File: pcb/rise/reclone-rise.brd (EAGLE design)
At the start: 85 x 56 mm, 13 parts, among them J1 MAGJACK, U1 6SLX16FTG256

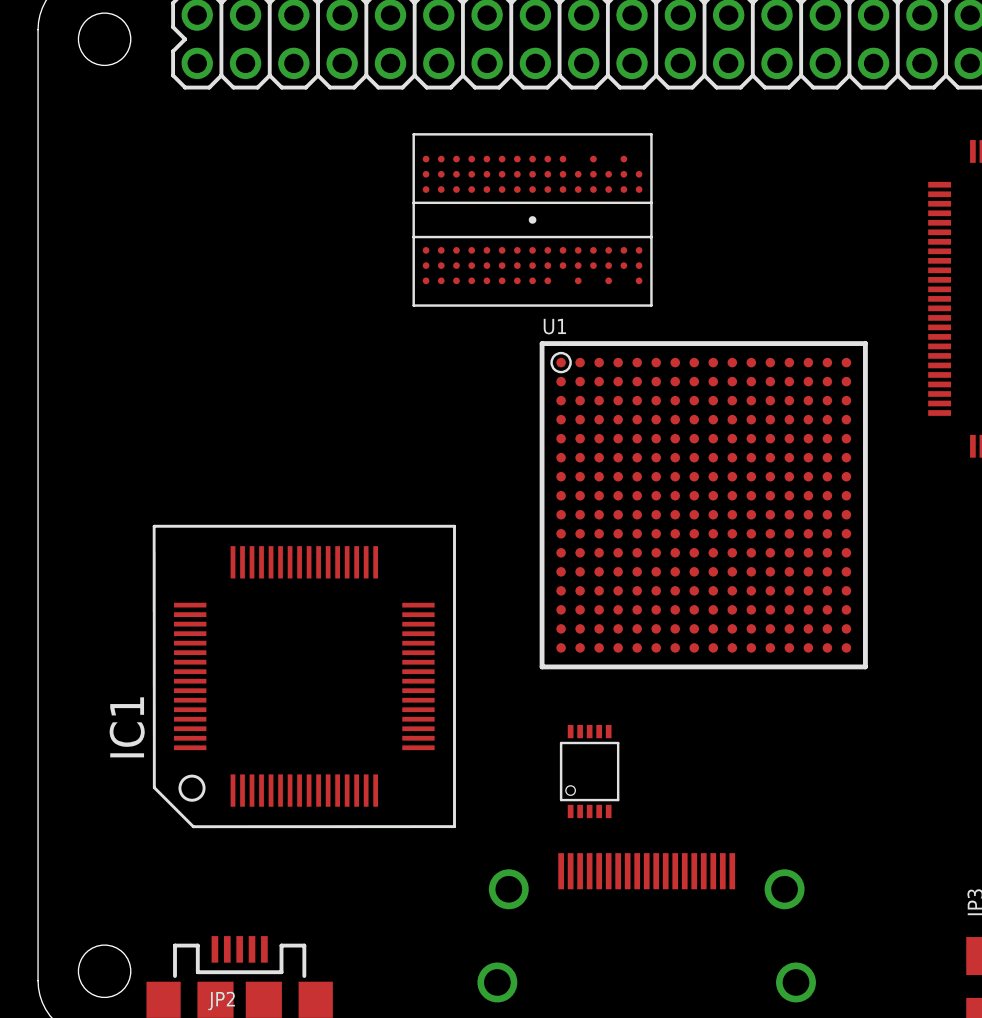
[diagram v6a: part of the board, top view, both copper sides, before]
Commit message: Added microSD socket as a placeholder
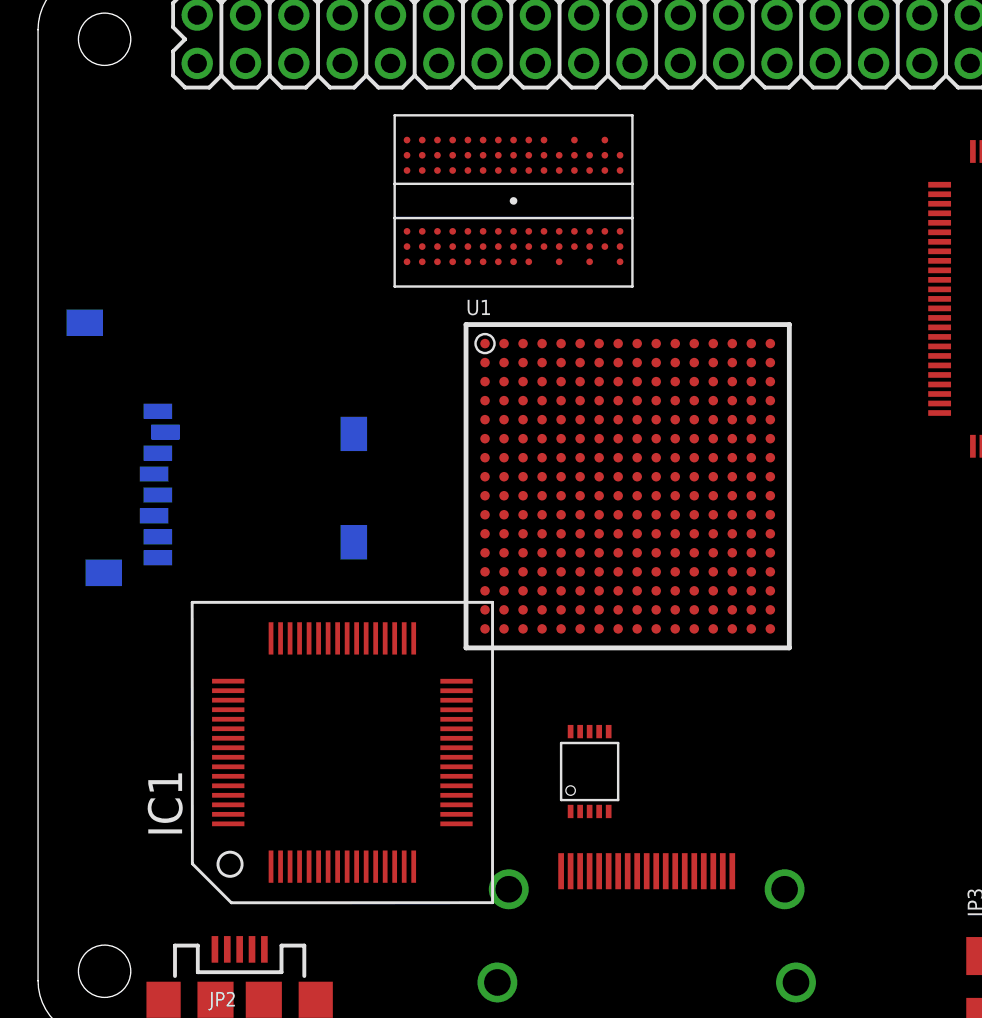
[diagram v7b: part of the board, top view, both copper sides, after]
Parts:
- added U2: USD-SOCKETNEW, SparkFun-Connectors:MICRO-SD-SOCKET-PP
- moved IC1 4.47 mm to (16.0, 15.0)
- moved U1 4.12 mm to (31.0, 29.0)
- moved U$5 1.41 mm to (25.0, 44.0)
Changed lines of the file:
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@@
 <element name="JP1" library="SparkFun-Connectors" package="2X20" value="M20X2" x="32.5" y="52.5" locked="yes"/>
 <element name="J1" library="SparkFun-Connectors" package="MAGJACK" value="MAGJACK" x="86" y="2.25" locked="yes" rot="R90"/>
-<element name="IC1" library="ftdichip-3" package="TQFP64-12X12" value="" x="14" y="19"/>
+<element name="IC1" library="ftdichip-3" package="TQFP64-12X12" value="" x="16" y="15"/>
 <element name="JP2" library="SparkFun-Connectors" package="USB-MICROB" value="USB-MICROB" x="10.6" y="2" locked="yes">
 <attribute name="PROD_ID" value="CONN-09505" x="10.6" y="2" size="1.778" layer="27" display="off"/>
@@
 <element name="U$2" library="reclone-rise" package="LQFP-48" value="DP83848C" x="57" y="23"/>
 <element name="U$3" library="reclone-rise" package="HDMI_A_SMT" value="HDMI_A" x="32" y="4" locked="yes" rot="R270"/>
-<element name="U1" library="xilinx_devices_V6" package="FT256" value="6SLX16FTG256" x="35" y="28"/>
+<element name="U1" library="xilinx_devices_V6" package="FT256" value="6SLX16FTG256" x="31" y="29"/>
 <element name="U$4" library="Gadgeteer" package="SHF105DSM_1" value="SHF105" x="76" y="46"/>
-<element name="U$5" library="reclone-rise" package="84-FBGA-9X12.5" value="MT47H128M16" x="26" y="43" rot="R90"/>
+<element name="U$5" library="reclone-rise" package="84-FBGA-9X12.5" value="MT47H128M16" x="25" y="44" rot="R90"/>
+<element name="U2" library="SparkFun-Connectors" package="MICRO-SD-SOCKET-PP" value="USD-SOCKETNEW" x="17" y="24" rot="MR270">
+<attribute name="PROD_ID" value="CONN-07820" x="17" y="24" size="1.778" layer="28" rot="MR270" display="off"/>
+</element>
 </elements>
 <signals>
@@
 <contactref element="U1" pad="T1"/>
 <contactref element="U1" pad="T16"/>
-<wire x1="16.7501" y1="25.0001" x2="20.0001" y2="19.25" width="0" layer="19" extent="1-1"/>
-<wire x1="10.7499" y1="25.0001" x2="16.7501" y2="25.0001" width="0" layer="19" extent="1-1"/>
-<wire x1="7.9999" y1="21.75" x2="10.7499" y2="25.0001" width="0" layer="19" extent="1-1"/>
-<wire x1="17.25" y1="12.9999" x2="20.0001" y2="19.25" width="0" layer="19" extent="1-1"/>
-<wire x1="15.25" y1="12.9999" x2="17.25" y2="12.9999" width="0" layer="19" extent="1-1"/>
-<wire x1="12.25" y1="12.9999" x2="15.25" y2="12.9999" width="0" layer="19" extent="1-1"/>
-<wire x1="10.25" y1="12.9999" x2="12.25" y2="12.9999" width="0" layer="19" extent="1-1"/>
-<wire x1="42.5" y1="35.5" x2="7.9999" y2="21.75" width="0" layer="19" extent="1-1"/>
-<wire x1="39.5" y1="32.5" x2="42.5" y2="35.5" width="0" layer="19" extent="1-1"/>
-<wire x1="37.5" y1="34.5" x2="39.5" y2="32.5" width="0" layer="19" extent="1-1"/>
-<wire x1="41.5" y1="29.5" x2="39.5" y2="32.5" width="0" layer="19" extent="1-1"/>
-<wire x1="38.5" y1="28.5" x2="41.5" y2="29.5" width="0" layer="19" extent="1-1"/>
-<wire x1="35.5" y1="28.5" x2="38.5" y2="28.5" width="0" layer="19" extent="1-1"/>
-<wire x1="34.5" y1="27.5" x2="35.5" y2="28.5" width="0" layer="19" extent="1-1"/>
-<wire x1="33.5" y1="28.5" x2="34.5" y2="27.5" width="0" layer="19" extent="1-1"/>
-<wire x1="33.5" y1="26.5" x2="34.5" y2="27.5" width="0" layer="19" extent="1-1"/>
-<wire x1="35.5" y1="26.5" x2="34.5" y2="27.5" width="0" layer="19" extent="1-1"/>
-<wire x1="34.5" y1="29.5" x2="35.5" y2="28.5" width="0" layer="19" extent="1-1"/>
-<wire x1="31.5" y1="27.5" x2="33.5" y2="28.5" width="0" layer="19" extent="1-1"/>
-<wire x1="34.5" y1="24.5" x2="33.5" y2="26.5" width="0" layer="19" extent="1-1"/>
-<wire x1="35.5" y1="31.5" x2="34.5" y2="29.5" width="0" layer="19" extent="1-1"/>
-<wire x1="28.5" y1="25.5" x2="31.5" y2="27.5" width="0" layer="19" extent="1-1"/>
-<wire x1="29.5" y1="22.5" x2="28.5" y2="25.5" width="0" layer="19" extent="1-1"/>
-<wire x1="27.5" y1="20.5" x2="29.5" y2="22.5" width="0" layer="19" extent="1-1"/>
-<wire x1="32.5" y1="21.5" x2="29.5" y2="22.5" width="0" layer="19" extent="1-1"/>
-<wire x1="28.5" y1="29.5" x2="31.5" y2="27.5" width="0" layer="19" extent="1-1"/>
-<wire x1="36.5" y1="21.5" x2="34.5" y2="24.5" width="0" layer="19" extent="1-1"/>
-<wire x1="33.5" y1="34.5" x2="35.5" y2="31.5" width="0" layer="19" extent="1-1"/>
-<wire x1="30.5" y1="32.5" x2="28.5" y2="29.5" width="0" layer="19" extent="1-1"/>
-<wire x1="39.5" y1="23.5" x2="36.5" y2="21.5" width="0" layer="19" extent="1-1"/>
-<wire x1="41.5" y1="25.5" x2="39.5" y2="23.5" width="0" layer="19" extent="1-1"/>
-<wire x1="27.5" y1="35.5" x2="30.5" y2="32.5" width="0" layer="19" extent="1-1"/>
-<wire x1="42.5" y1="20.5" x2="39.5" y2="23.5" width="0" layer="19" extent="1-1"/>
+<wire x1="18.7501" y1="21.0001" x2="22.0001" y2="15.25" width="0" layer="19" extent="1-1"/>
+<wire x1="12.7499" y1="21.0001" x2="18.7501" y2="21.0001" width="0" layer="19" extent="1-1"/>
+<wire x1="9.9999" y1="17.75" x2="12.7499" y2="21.0001" width="0" layer="19" extent="1-1"/>
+<wire x1="19.25" y1="8.9999" x2="22.0001" y2="15.25" width="0" layer="19" extent="1-1"/>
+<wire x1="17.25" y1="8.9999" x2="19.25" y2="8.9999" width="0" layer="19" extent="1-1"/>
+<wire x1="14.25" y1="8.9999" x2="17.25" y2="8.9999" width="0" layer="19" extent="1-1"/>
+<wire x1="12.25" y1="8.9999" x2="14.25" y2="8.9999" width="0" layer="19" extent="1-1"/>
+<wire x1="38.5" y1="36.5" x2="9.9999" y2="17.75" width="0" layer="19" extent="1-1"/>
+<wire x1="35.5" y1="33.5" x2="38.5" y2="36.5" width="0" layer="19" extent="1-1"/>
+<wire x1="33.5" y1="35.5" x2="35.5" y2="33.5" width="0" layer="19" extent="1-1"/>
+<wire x1="37.5" y1="30.5" x2="35.5" y2="33.5" width="0" layer="19" extent="1-1"/>
+<wire x1="34.5" y1="29.5" x2="37.5" y2="30.5" width="0" layer="19" extent="1-1"/>
+<wire x1="31.5" y1="29.5" x2="34.5" y2="29.5" width="0" layer="19" extent="1-1"/>
+<wire x1="30.5" y1="28.5" x2="31.5" y2="29.5" width="0" layer="19" extent="1-1"/>
+<wire x1="29.5" y1="29.5" x2="30.5" y2="28.5" width="0" layer="19" extent="1-1"/>
+<wire x1="29.5" y1="27.5" x2="30.5" y2="28.5" width="0" layer="19" extent="1-1"/>
+<wire x1="31.5" y1="27.5" x2="30.5" y2="28.5" width="0" layer="19" extent="1-1"/>
+<wire x1="30.5" y1="30.5" x2="31.5" y2="29.5" width="0" layer="19" extent="1-1"/>
+<wire x1="27.5" y1="28.5" x2="29.5" y2="29.5" width="0" layer="19" extent="1-1"/>
+<wire x1="30.5" y1="25.5" x2="29.5" y2="27.5" width="0" layer="19" extent="1-1"/>
+<wire x1="31.5" y1="32.5" x2="30.5" y2="30.5" width="0" layer="19" extent="1-1"/>
+<wire x1="24.5" y1="26.5" x2="27.5" y2="28.5" width="0" layer="19" extent="1-1"/>
+<wire x1="25.5" y1="23.5" x2="24.5" y2="26.5" width="0" layer="19" extent="1-1"/>
+<wire x1="23.5" y1="21.5" x2="25.5" y2="23.5" width="0" layer="19" extent="1-1"/>
+<wire x1="28.5" y1="22.5" x2="25.5" y2="23.5" width="0" layer="19" extent="1-1"/>
+<wire x1="24.5" y1="30.5" x2="27.5" y2="28.5" width="0" layer="19" extent="1-1"/>
+<wire x1="32.5" y1="22.5" x2="30.5" y2="25.5" width="0" layer="19" extent="1-1"/>
+<wire x1="29.5" y1="35.5" x2="31.5" y2="32.5" width="0" layer="19" extent="1-1"/>
+<wire x1="26.5" y1="33.5" x2="24.5" y2="30.5" width="0" layer="19" extent="1-1"/>
+<wire x1="35.5" y1="24.5" x2="32.5" y2="22.5" width="0" layer="19" extent="1-1"/>
+<wire x1="37.5" y1="26.5" x2="35.5" y2="24.5" width="0" layer="19" extent="1-1"/>
+<wire x1="23.5" y1="36.5" x2="26.5" y2="33.5" width="0" layer="19" extent="1-1"/>
+<wire x1="38.5" y1="21.5" x2="35.5" y2="24.5" width="0" layer="19" extent="1-1"/>
 </signal>
 <signal name="AGND">
@@
 <contactref element="IC1" pad="37"/>
 <contactref element="IC1" pad="64"/>
-<wire x1="15.7499" y1="12.9999" x2="15.7501" y2="25.0001" width="0" layer="19" extent="1-1"/>
-<wire x1="7.9999" y1="15.2499" x2="15.7499" y2="12.9999" width="0" layer="19" extent="1-1"/>
+<wire x1="17.7499" y1="8.9999" x2="17.7501" y2="21.0001" width="0" layer="19" extent="1-1"/>
+<wire x1="9.9999" y1="11.2499" x2="17.7499" y2="8.9999" width="0" layer="19" extent="1-1"/>
 </signal>
 <signal name="VCCIO">
@@
 <contactref element="IC1" pad="42"/>
 <contactref element="IC1" pad="56"/>
-<wire x1="20.0001" y1="16.7501" x2="20.0001" y2="22.2469" width="0" layer="19" extent="1-1"/>
-<wire x1="13.25" y1="25.0001" x2="20.0001" y2="22.2469" width="0" layer="19" extent="1-1"/>
-<wire x1="7.9999" y1="19.2501" x2="13.25" y2="25.0001" width="0" layer="19" extent="1-1"/>
+<wire x1="22.0001" y1="12.7501" x2="22.0001" y2="18.2469" width="0" layer="19" extent="1-1"/>
+<wire x1="15.25" y1="21.0001" x2="22.0001" y2="18.2469" width="0" layer="19" extent="1-1"/>
+<wire x1="9.9999" y1="15.2501" x2="15.25" y2="21.0001" width="0" layer="19" extent="1-1"/>
 </signal>
 <signal name="VPLL">

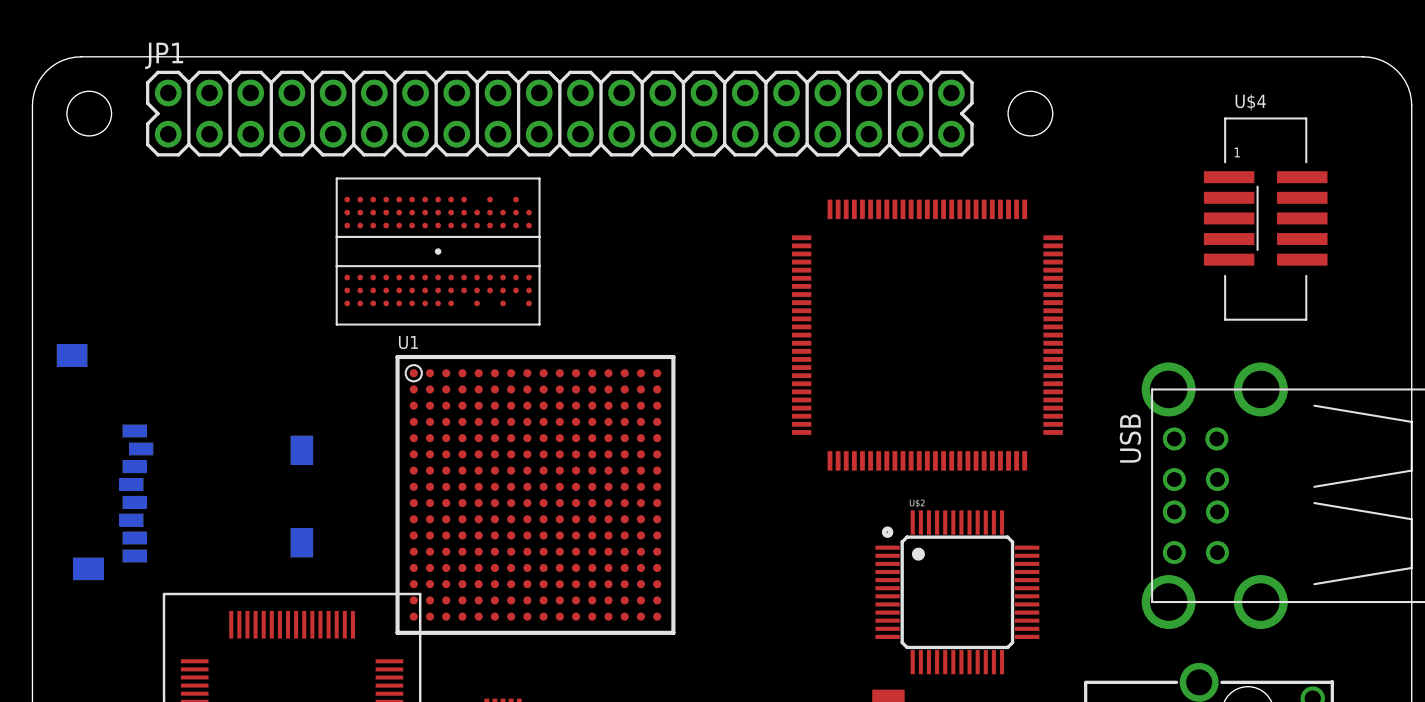
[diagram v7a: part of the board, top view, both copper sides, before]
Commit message: Added draft FPC15-0.5 package for FPC vertical mount connector for camera and lcd
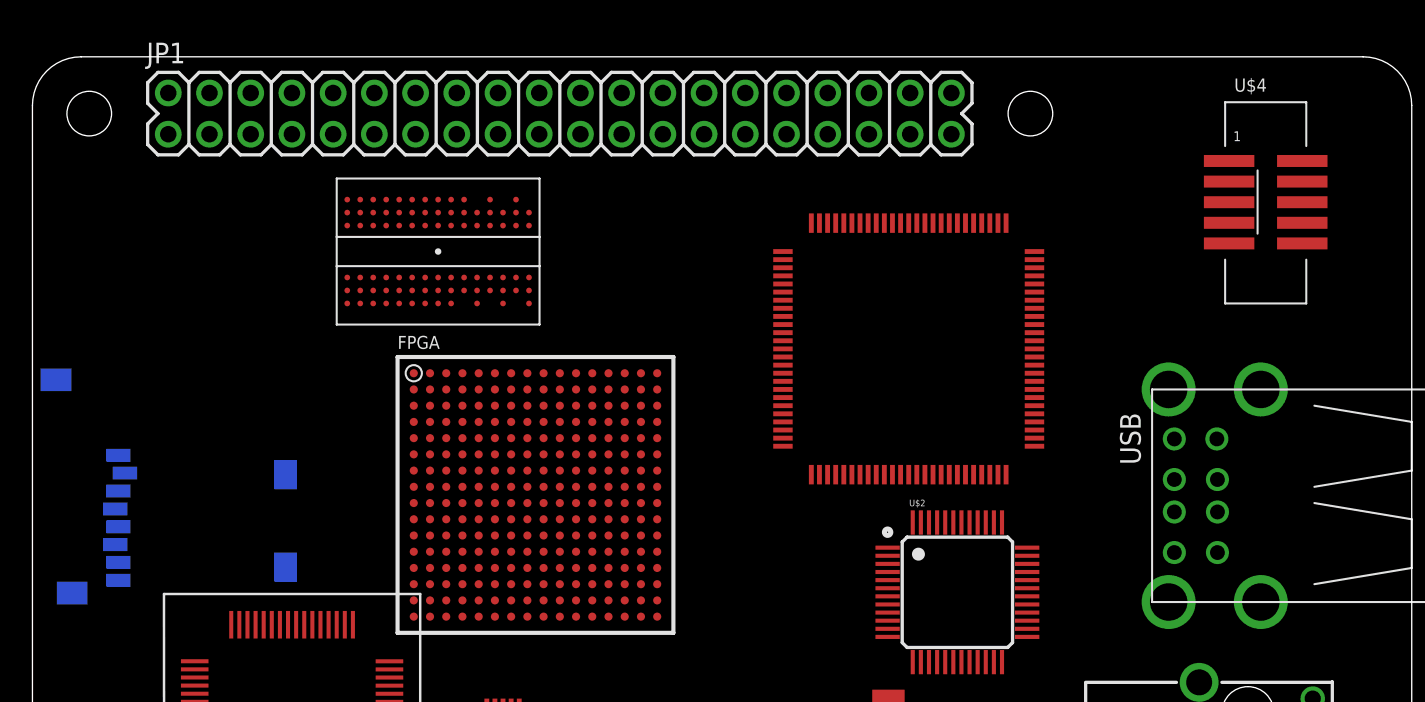
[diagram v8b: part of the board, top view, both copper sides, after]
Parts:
- moved MCU 10.0 mm to (54.0, 38.0)
- moved U2 1.80 mm to (16.0, 22.5)
- moved U$4 1.00 mm to (76.0, 47.0)
- renumbered U1 to FPGA
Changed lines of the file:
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@@
 <elements>
 <element name="USB" library="reclone-rise" package="USB-A-2H" value="USB_A_2H" x="69" y="29" locked="yes" rot="R180"/>
-<element name="MCU" library="reclone-rise" package="LQFP-100" value="STM32F407VGT6" x="48" y="46" rot="R270"/>
+<element name="MCU" library="reclone-rise" package="LQFP-100" value="STM32F407VGT6" x="54" y="38" rot="R270"/>
 <element name="JP1" library="SparkFun-Connectors" package="2X20" value="M20X2" x="32.5" y="52.5" locked="yes"/>
 <element name="J1" library="SparkFun-Connectors" package="MAGJACK" value="MAGJACK" x="86" y="2.25" locked="yes" rot="R90"/>
@@
 <element name="U$2" library="reclone-rise" package="LQFP-48" value="DP83848C" x="57" y="23"/>
 <element name="U$3" library="reclone-rise" package="HDMI_A_SMT" value="HDMI_A" x="32" y="4" locked="yes" rot="R270"/>
-<element name="U1" library="xilinx_devices_V6" package="FT256" value="6SLX16FTG256" x="31" y="29"/>
-<element name="U$4" library="Gadgeteer" package="SHF105DSM_1" value="SHF105" x="76" y="46"/>
+<element name="FPGA" library="xilinx_devices_V6" package="FT256" value="6SLX16FTG256" x="31" y="29"/>
+<element name="U$4" library="Gadgeteer" package="SHF105DSM_1" value="SHF105" x="76" y="47" locked="yes"/>
 <element name="U$5" library="reclone-rise" package="84-FBGA-9X12.5" value="MT47H128M16" x="25" y="44" rot="R90"/>
-<element name="U2" library="SparkFun-Connectors" package="MICRO-SD-SOCKET-PP" value="USD-SOCKETNEW" x="17" y="24" rot="MR270">
-<attribute name="PROD_ID" value="CONN-07820" x="17" y="24" size="1.778" layer="28" rot="MR270" display="off"/>
+<element name="U2" library="SparkFun-Connectors" package="MICRO-SD-SOCKET-PP" value="USD-SOCKETNEW" x="16" y="22.5" locked="yes" rot="MR270">
+<attribute name="PROD_ID" value="CONN-07820" x="16" y="22.5" size="1.778" layer="28" rot="MR270" display="off"/>
 </element>
 </elements>
@@
 <contactref element="IC1" pad="47"/>
 <contactref element="IC1" pad="51"/>
-<contactref element="U1" pad="A1"/>
-<contactref element="U1" pad="A16"/>
-<contactref element="U1" pad="B7"/>
-<contactref element="U1" pad="B11"/>
-<contactref element="U1" pad="D4"/>
-<contactref element="U1" pad="D13"/>
-<contactref element="U1" pad="E9"/>
-<contactref element="U1" pad="G2"/>
-<contactref element="U1" pad="G8"/>
-<contactref element="U1" pad="G15"/>
-<contactref element="U1" pad="H7"/>
-<contactref element="U1" pad="H9"/>
-<contactref element="U1" pad="H12"/>
-<contactref element="U1" pad="J5"/>
-<contactref element="U1" pad="J8"/>
-<contactref element="U1" pad="K7"/>
-<contactref element="U1" pad="K9"/>
-<contactref element="U1" pad="L2"/>
-<contactref element="U1" pad="L15"/>
-<contactref element="U1" pad="M8"/>
-<contactref element="U1" pad="N13"/>
-<contactref element="U1" pad="P3"/>
-<contactref element="U1" pad="R6"/>
-<contactref element="U1" pad="R10"/>
-<contactref element="U1" pad="T1"/>
-<contactref element="U1" pad="T16"/>
+<contactref element="FPGA" pad="A1"/>
+<contactref element="FPGA" pad="A16"/>
+<contactref element="FPGA" pad="B7"/>
+<contactref element="FPGA" pad="B11"/>
+<contactref element="FPGA" pad="D4"/>
+<contactref element="FPGA" pad="D13"/>
+<contactref element="FPGA" pad="E9"/>
+<contactref element="FPGA" pad="G2"/>
+<contactref element="FPGA" pad="G8"/>
+<contactref element="FPGA" pad="G15"/>
+<contactref element="FPGA" pad="H7"/>
+<contactref element="FPGA" pad="H9"/>
+<contactref element="FPGA" pad="H12"/>
+<contactref element="FPGA" pad="J5"/>
+<contactref element="FPGA" pad="J8"/>
+<contactref element="FPGA" pad="K7"/>
+<contactref element="FPGA" pad="K9"/>
+<contactref element="FPGA" pad="L2"/>
+<contactref element="FPGA" pad="L15"/>
+<contactref element="FPGA" pad="M8"/>
+<contactref element="FPGA" pad="N13"/>
+<contactref element="FPGA" pad="P3"/>
+<contactref element="FPGA" pad="R6"/>
+<contactref element="FPGA" pad="R10"/>
+<contactref element="FPGA" pad="T1"/>
+<contactref element="FPGA" pad="T16"/>
 <wire x1="18.7501" y1="21.0001" x2="22.0001" y2="15.25" width="0" layer="19" extent="1-1"/>
 <wire x1="12.7499" y1="21.0001" x2="18.7501" y2="21.0001" width="0" layer="19" extent="1-1"/>
